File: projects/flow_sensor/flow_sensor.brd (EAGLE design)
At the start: 40 x 49.8 mm, 91 parts, among them IC1 TPS61201, IC2 TPS61201, IC3 MIC5219BM5, J5 455-1750-1-ND

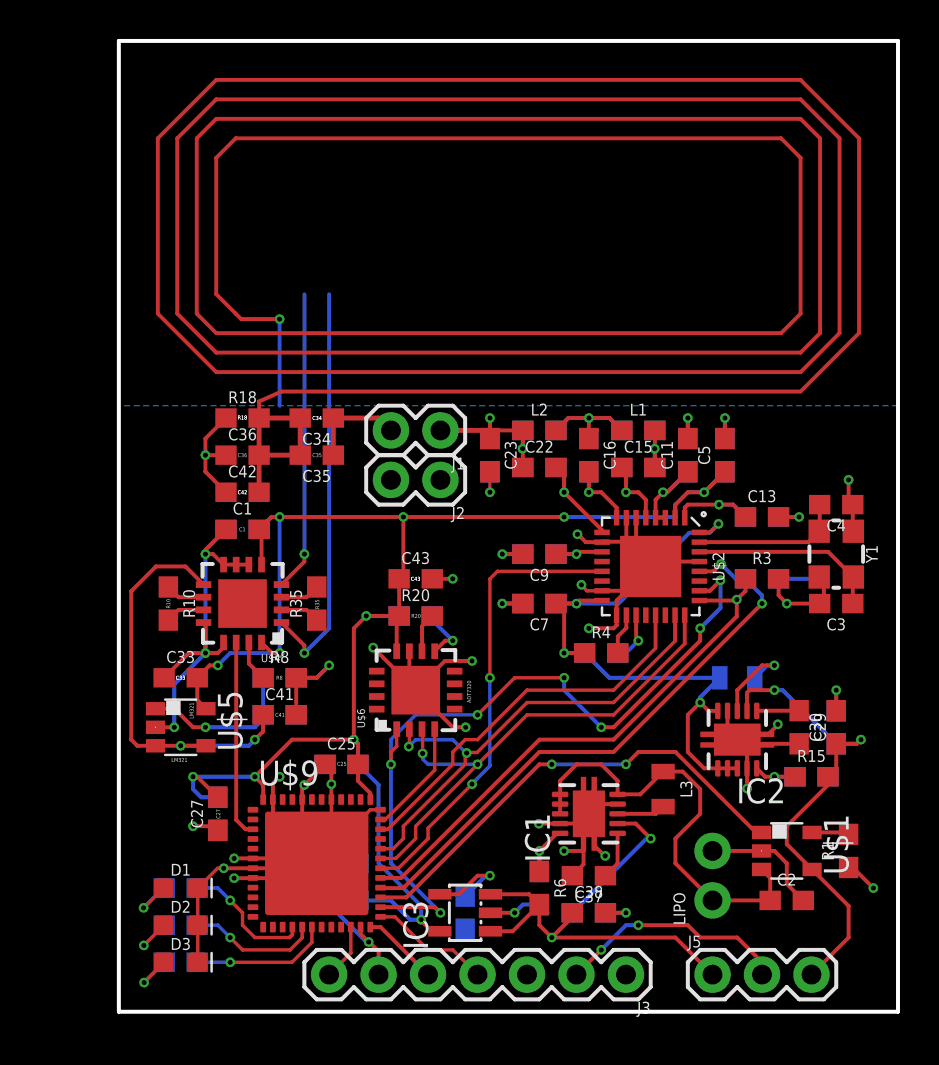
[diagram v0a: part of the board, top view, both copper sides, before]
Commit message: Touched up board V1.0, added labels
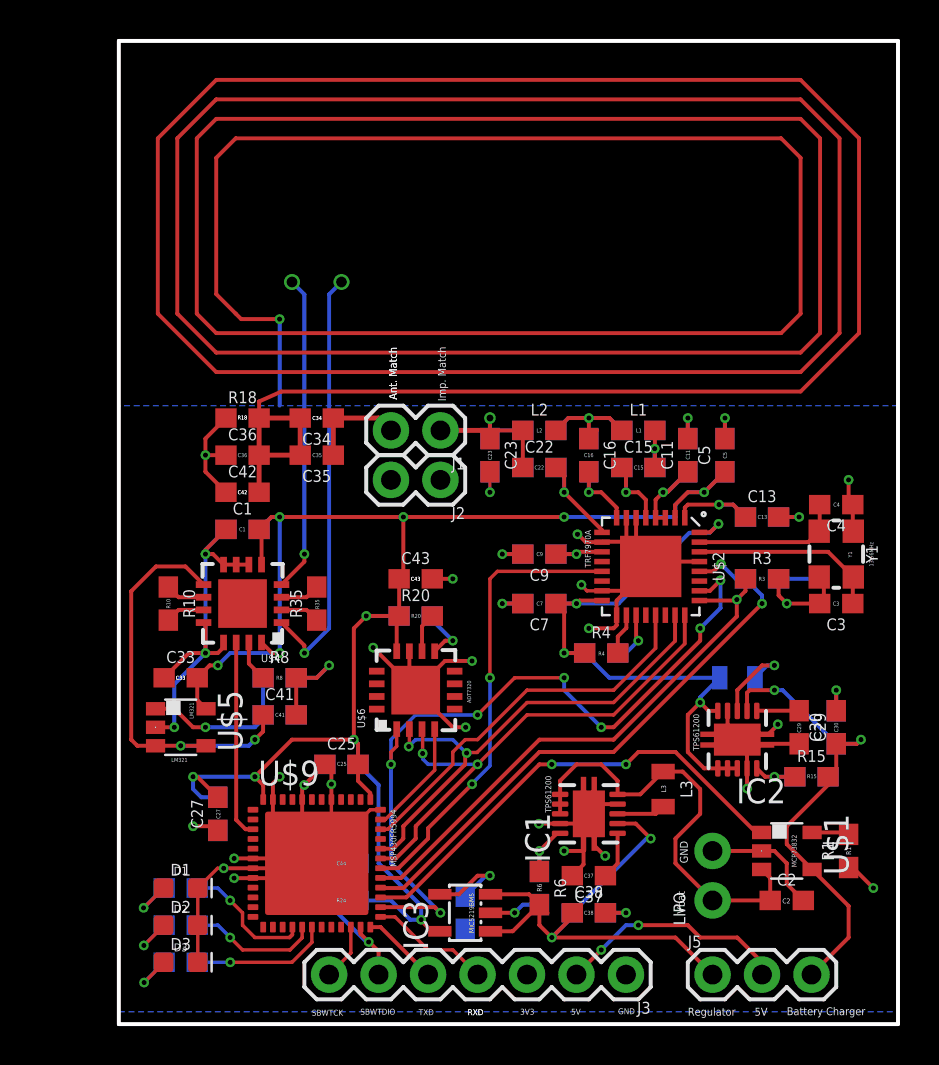
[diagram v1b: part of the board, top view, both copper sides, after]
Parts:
- IC1, IC2: value TPS61201 -> TPS61200
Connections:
- net COM_EN renamed COMMS_EN
- net COM_EN2 renamed COMMS_EN2
- net COM_SS renamed COMMS_SS
- net IRQ renamed COMMS_IRQ
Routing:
- net N$29: track 15.4 -> 16.3 mm, vias 1 -> 2
- net N$28: track 21.0 -> 21.9 mm, vias 1 -> 2
- net ANT: track 10.1 -> 10.5 mm, vias 2 -> 1
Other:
- board size 40 x 49.8 mm -> 40 x 50.5 mm
- board text added: "13.56MHz"
- board text added: "3V3"
- board text added: "5V"
- board text added: "Ant. Match"
- board text added: "Battery Charger"
- board text added: "Board V1.0"
- board text added: "C10"
- board text added: "C11"
- board text added: "C12"
- board text added: "C13"
- board text added: "C14"
- board text added: "C15"
- board text added: "C16"
- board text added: "C17"
- board text added: "C18"
- board text added: "C19"
- board text added: "C2"
- board text added: "C20"
- board text added: "C21"
- board text added: "C22"
- board text added: "C23"
- board text added: "C24"
- board text added: "C26"
- board text added: "C28"
- board text added: "C29"
- board text added: "C3"
- board text added: "C30"
- board text added: "C31"
- board text added: "C32"
- board text added: "C37"
- board text added: "C38"
- board text added: "C39"
- board text added: "C4"
- board text added: "C40"
- board text added: "C44"
- board text added: "C5"
- board text added: "C6"
- board text added: "C7"
- board text added: "C8"
- board text added: "C9"
- board text added: "D1"
- board text added: "D2"
- board text added: "D3"
- board text added: "Flow_Sensor Senior Design Project"
- board text added: "GND"
- board text added: "Imp. Match"
- board text added: "L1"
- board text added: "L2"
- board text added: "L3"
- board text added: "L4"
- board text added: "MCP73832"
- board text added: "MIC5219BM5"
- board text added: "MSP430FR5994"
- board text added: "R1"
- board text added: "R15"
- board text added: "R16"
- board text added: "R17"
- board text added: "R19"
- board text added: "R2"
- board text added: "R21"
- board text added: "R22"
- board text added: "R23"
- board text added: "R24"
- board text added: "R3"
- board text added: "R4"
- board text added: "R5"
- board text added: "R6"
- board text added: "R7"
- board text added: "R9"
- board text added: "RXD"
- board text added: "Regulator"
- board text added: "SBWTCK"
- board text added: "SBWTDIO"
- board text added: "TPS61200"
- board text added: "TRF7970A"
- board text added: "TXD"
- board text added: "Vbat"
- board text added: "Y1"

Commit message: Finalized Board Size, touched up labels
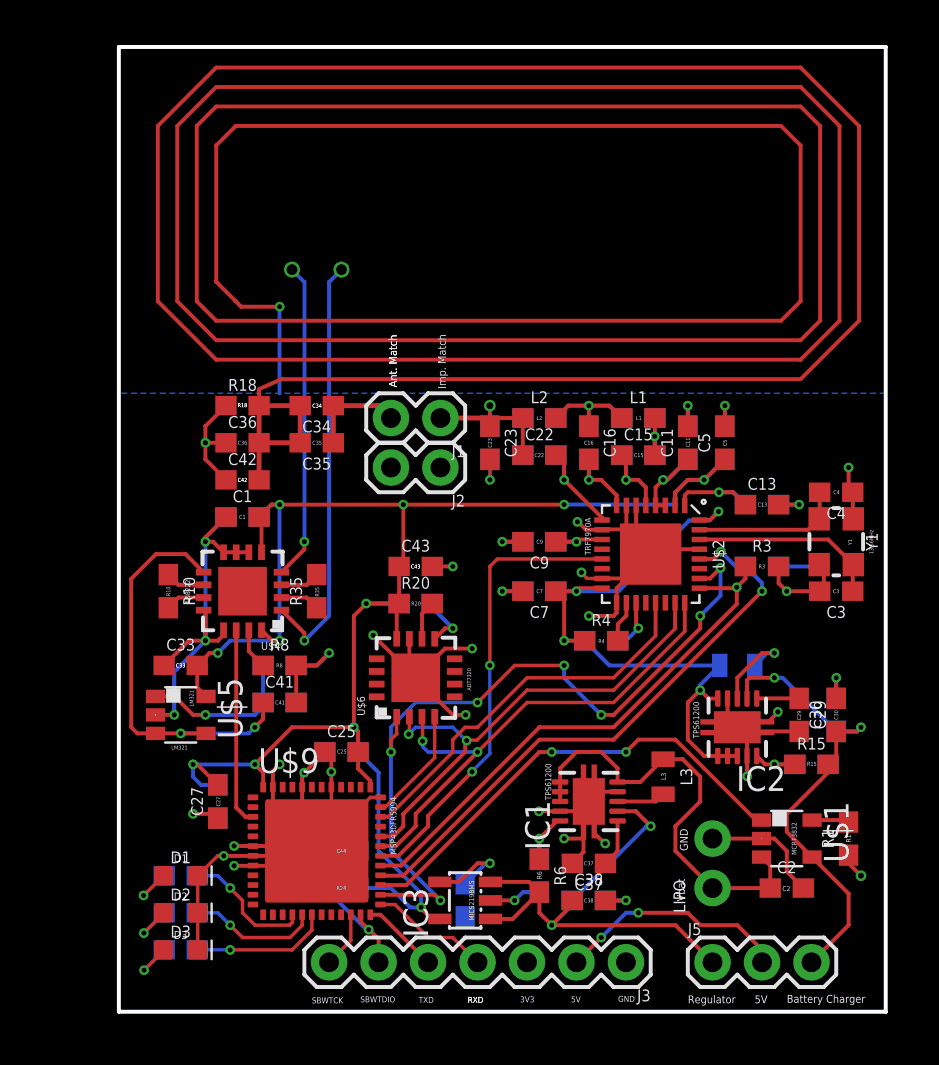
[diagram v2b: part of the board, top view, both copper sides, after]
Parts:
- moved C11 0.64 mm to (29.2, 29.2)
- moved C12 0.64 mm to (29.2, 29.2)
- moved C13 0.64 mm to (33.0, 26.0)
- moved C14 0.64 mm to (33.0, 26.0)
- moved C16 0.64 mm to (24.1, 29.2)
- moved C17 0.64 mm to (24.1, 29.2)
- moved C19 0.64 mm to (26.7, 30.5)
- moved C20 0.64 mm to (21.6, 30.5)
- moved C23 0.64 mm to (19.1, 29.2)
- moved C24 0.64 mm to (19.1, 29.2)
- moved C25 0.64 mm to (11.4, 13.3)
- moved C26 0.64 mm to (11.4, 13.3)
- moved C3 0.64 mm to (36.8, 21.6)
- moved C33 0.64 mm to (3.17, 17.8)
- moved C35 0.64 mm to (10.2, 29.2)
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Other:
- board size 40 x 50.5 mm -> 39.4 x 49.5 mm
- board text added: "AD8222"

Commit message: starting v2.0
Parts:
- removed R11, R12, R13, R14: 1.5k, SparkFun-Resistors:0603
- added J4: (no value), SparkFun-Connectors:1X02_NO_SILK
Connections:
- net GND: no longer R13.2, R14.2
- net N$28: now also J4.2; no longer R11.2, R14.1
- net N$29: now also J4.1; no longer R12.2, R13.1
- net VCC: no longer R11.1, R12.1
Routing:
- net GND: track 525.9 -> 556.0 mm
- net N$29: vias 2 -> 1
- net N$28: vias 2 -> 1
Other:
- board text added: "+"
- board text added: "Flow Sensor Senior Design Project"
- board text added: "Sensor Input"
- board text added: "_"
- board text removed: "Flow_Sensor Senior Design Project"

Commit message: added stuff for board v2
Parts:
- added R11: 180k, SparkFun-Resistors:0603
- R1: value 20k -> 67k
- R15: value 1M -> 1.6M
- R16: value 180k -> 200k
- R17: value 180k -> 300k
- R21, R22: value 680 -> 47
- R23: value 680 -> 20
- R6: value 1M -> 1.2M
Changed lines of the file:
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@@
 <layer number="23" name="tOrigins" color="15" fill="1" visible="yes" active="yes"/>
 <layer number="24" name="bOrigins" color="15" fill="1" visible="yes" active="yes"/>
-<layer number="25" name="tNames" color="7" fill="1" visible="no" active="yes"/>
-<layer number="26" name="bNames" color="7" fill="1" visible="no" active="yes"/>
-<layer number="27" name="tValues" color="7" fill="1" visible="no" active="yes"/>
-<layer number="28" name="bValues" color="7" fill="1" visible="no" active="yes"/>
+<layer number="25" name="tNames" color="7" fill="1" visible="yes" active="yes"/>
+<layer number="26" name="bNames" color="7" fill="1" visible="yes" active="yes"/>
+<layer number="27" name="tValues" color="7" fill="1" visible="yes" active="yes"/>
+<layer number="28" name="bValues" color="7" fill="1" visible="yes" active="yes"/>
 <layer number="29" name="tStop" color="7" fill="3" visible="no" active="yes"/>
 <layer number="30" name="bStop" color="7" fill="6" visible="no" active="yes"/>
@@
 <layer number="37" name="tTest" color="7" fill="1" visible="no" active="yes"/>
 <layer number="38" name="bTest" color="7" fill="1" visible="no" active="yes"/>
-<layer number="39" name="tKeepout" color="4" fill="11" visible="no" active="yes"/>
-<layer number="40" name="bKeepout" color="1" fill="11" visible="no" active="yes"/>
-<layer number="41" name="tRestrict" color="4" fill="10" visible="no" active="yes"/>
-<layer number="42" name="bRestrict" color="1" fill="10" visible="no" active="yes"/>
+<layer number="39" name="tKeepout" color="4" fill="11" visible="yes" active="yes"/>
+<layer number="40" name="bKeepout" color="1" fill="11" visible="yes" active="yes"/>
+<layer number="41" name="tRestrict" color="4" fill="10" visible="yes" active="yes"/>
+<layer number="42" name="bRestrict" color="1" fill="10" visible="yes" active="yes"/>
 <layer number="43" name="vRestrict" color="2" fill="10" visible="no" active="yes"/>
-<layer number="44" name="Drills" color="7" fill="1" visible="no" active="yes"/>
-<layer number="45" name="Holes" color="7" fill="1" visible="no" active="yes"/>
+<layer number="44" name="Drills" color="7" fill="1" visible="yes" active="yes"/>
+<layer number="45" name="Holes" color="7" fill="1" visible="yes" active="yes"/>
 <layer number="46" name="Milling" color="3" fill="1" visible="no" active="yes"/>
 <layer number="47" name="Measures" color="7" fill="1" visible="no" active="yes"/>
@@
 <layer number="49" name="Reference" color="7" fill="1" visible="no" active="yes"/>
 <layer number="50" name="dxf" color="7" fill="1" visible="no" active="no"/>
-<layer number="51" name="tDocu" color="7" fill="1" visible="no" active="yes"/>
-<layer number="52" name="bDocu" color="7" fill="1" visible="no" active="yes"/>
+<layer number="51" name="tDocu" color="7" fill="1" visible="yes" active="yes"/>
+<layer number="52" name="bDocu" color="7" fill="1" visible="yes" active="yes"/>
 <layer number="53" name="tGND_GNDA" color="7" fill="9" visible="no" active="no"/>
 <layer number="54" name="bGND_GNDA" color="1" fill="9" visible="no" active="no"/>
@@
 </element>
 <element name="LIPO" library="SparkFun-Connectors" package="1X02_NO_SILK" value="" x="30.48" y="6.35" rot="R90"/>
-<element name="R1" library="SparkFun-Resistors" package="0603" value="20k" x="37.465" y="8.89" rot="R90">
+<element name="R1" library="SparkFun-Resistors" package="0603" value="67k" x="37.465" y="8.89" rot="R90">
 <attribute name="PROD_ID" value="RES-09383" x="37.465" y="8.89" size="1.778" layer="27" rot="R90" display="off"/>
 </element>
@@
 <attribute name="PROD_ID" value="RES-11228" x="2.54" y="21.59" size="1.778" layer="27" rot="R270" display="off"/>
 </element>
-<element name="R15" library="SparkFun-Resistors" package="0603" value="1M" x="35.56" y="12.7">
+<element name="R15" library="SparkFun-Resistors" package="0603" value="1.6M" x="35.56" y="12.7">
 <attribute name="PROD_ID" value="RES-07868" x="35.56" y="12.7" size="1.778" layer="27" display="off"/>
 </element>
-<element name="R16" library="SparkFun-Resistors" package="0603" value="180k" x="35.56" y="12.7" rot="MR0">
+<element name="R16" library="SparkFun-Resistors" package="0603" value="200k" x="35.56" y="12.7" rot="MR0">
 <attribute name="PROD_ID" value="RES-08788" x="35.56" y="12.7" size="1.778" layer="28" rot="MR0" display="off"/>
 </element>
-<element name="R17" library="SparkFun-Resistors" package="0603" value="180k" x="17.78" y="5.715" rot="MR90">
+<element name="R17" library="SparkFun-Resistors" package="0603" value="300k" x="17.78" y="5.715" rot="MR90">
 <attribute name="PROD_ID" value="RES-08788" x="17.78" y="5.715" size="1.778" layer="28" rot="MR90" display="off"/>
 </element>
@@
 <attribute name="PROD_ID" value="RES-00824" x="24.765" y="19.05" size="1.778" layer="28" rot="MR180" display="off"/>
 </element>
-<element name="R6" library="SparkFun-Resistors" package="0603" value="1M" x="21.59" y="6.985" rot="R270">
+<element name="R6" library="SparkFun-Resistors" package="0603" value="1.2M" x="21.59" y="6.985" rot="R270">
 <attribute name="PROD_ID" value="RES-07868" x="21.59" y="6.985" size="1.778" layer="27" rot="R270" display="off"/>
 </element>
@@
 <element name="D2" library="SparkFun-LED" package="LED-0603" value="" x="3.175" y="5.08"/>
 <element name="D3" library="SparkFun-LED" package="LED-0603" value="" x="3.175" y="3.175"/>
-<element name="R21" library="SparkFun-Resistors" package="0603" value="680" x="3.175" y="6.985" rot="MR180">
+<element name="R21" library="SparkFun-Resistors" package="0603" value="47" x="3.175" y="6.985" rot="MR180">
 <attribute name="PROD_ID" value="RES-09333" x="3.175" y="6.985" size="0.2032" layer="28" rot="MR180" display="off"/>
 </element>
-<element name="R22" library="SparkFun-Resistors" package="0603" value="680" x="3.175" y="5.08" rot="MR180">
+<element name="R22" library="SparkFun-Resistors" package="0603" value="47" x="3.175" y="5.08" rot="MR180">
 <attribute name="PROD_ID" value="RES-09333" x="3.175" y="5.08" size="0.2032" layer="28" rot="MR180" display="off"/>
 </element>
-<element name="R23" library="SparkFun-Resistors" package="0603" value="680" x="3.175" y="3.175" rot="MR180">
+<element name="R23" library="SparkFun-Resistors" package="0603" value="20" x="3.175" y="3.175" rot="MR180">
 <attribute name="PROD_ID" value="RES-09333" x="3.175" y="3.175" size="0.2032" layer="28" rot="MR180" display="off"/>
 </element>
@@
 </element>
 <element name="J4" library="SparkFun-Connectors" package="1X02_NO_SILK" value="" x="8.89" y="38.1"/>
+<element name="R11" library="SparkFun-Resistors" package="0603" value="180k" x="2.54" y="-8.89">
+<attribute name="PROD_ID" value="RES-08788" x="2.54" y="-8.89" size="1.778" layer="27" display="off"/>
+</element>
 </elements>
 <signals>
@@
 <wire x1="37.465" y1="7.62" x2="38.1" y2="6.985" width="0.2032" layer="1"/>
 <via x="38.1" y="6.985" extent="1-16" drill="0.3"/>
-<polygon width="0.2032" layer="16" isolate="0.254">
+<polygon width="0.2032" layer="16" isolate="0.127">
 <vertex x="0" y="0"/>
 <vertex x="39.37" y="0"/>
@@
 <wire x1="7.211646875" y1="31.745815625" x2="7.89248125" y2="32.42665" width="0.2032" layer="1" curve="-90"/>
 <wire x1="7.89248125" y1="32.42665" x2="8.23645" y2="32.42665" width="0.2032" layer="1"/>
-<wire x1="27.52" y1="30.48" x2="24.13" y2="30.06" width="0" layer="19" extent="16-16"/>
 </signal>
 <signal name="CHG_STAT">

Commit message: Added MSP430F5229 to replace MSP430FR5994
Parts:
- added U$3: F552X---PN80, TI_MSP430_v16:PN80
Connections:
- new net 11: U$3.11
- new net 14: U$3.14
- new net 18: U$3.18
- new net 19: U$3.19
- new net 20: U$3.20
- new net 49: U$3.49
- new net 50: U$3.50
- new net 61: U$3.61
- new net 65: U$3.65
- new net 66: U$3.66
- new net 67: U$3.67
- new net 68: U$3.68
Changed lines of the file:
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@@
 <attribute name="PROD_ID" value="RES-08788" x="2.54" y="-8.89" size="1.778" layer="27" display="off"/>
 </element>
+<element name="U$3" library="TI_MSP430_v16" package="PN80" value="F552X---PN80" x="8.255" y="-19.05"/>
 </elements>
 <signals>
@@
 <wire x1="9.525" y1="23.74" x2="8.35" y2="22.565" width="0.2032" layer="1"/>
 </signal>
+<signal name="68">
+<contactref element="U$3" pad="68"/>
+</signal>
+<signal name="67">
+<contactref element="U$3" pad="67"/>
+</signal>
+<signal name="66">
+<contactref element="U$3" pad="66"/>
+</signal>
+<signal name="65">
+<contactref element="U$3" pad="65"/>
+</signal>
+<signal name="61">
+<contactref element="U$3" pad="61"/>
+</signal>
+<signal name="50">
+<contactref element="U$3" pad="50"/>
+</signal>
+<signal name="49">
+<contactref element="U$3" pad="49"/>
+</signal>
+<signal name="20">
+<contactref element="U$3" pad="20"/>
+</signal>
+<signal name="19">
+<contactref element="U$3" pad="19"/>
+</signal>
+<signal name="18">
+<contactref element="U$3" pad="18"/>
+</signal>
+<signal name="14">
+<contactref element="U$3" pad="14"/>
+</signal>
+<signal name="11">
+<contactref element="U$3" pad="11"/>
+</signal>
 </signals>
